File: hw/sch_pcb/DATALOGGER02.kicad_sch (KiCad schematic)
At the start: 0 parts

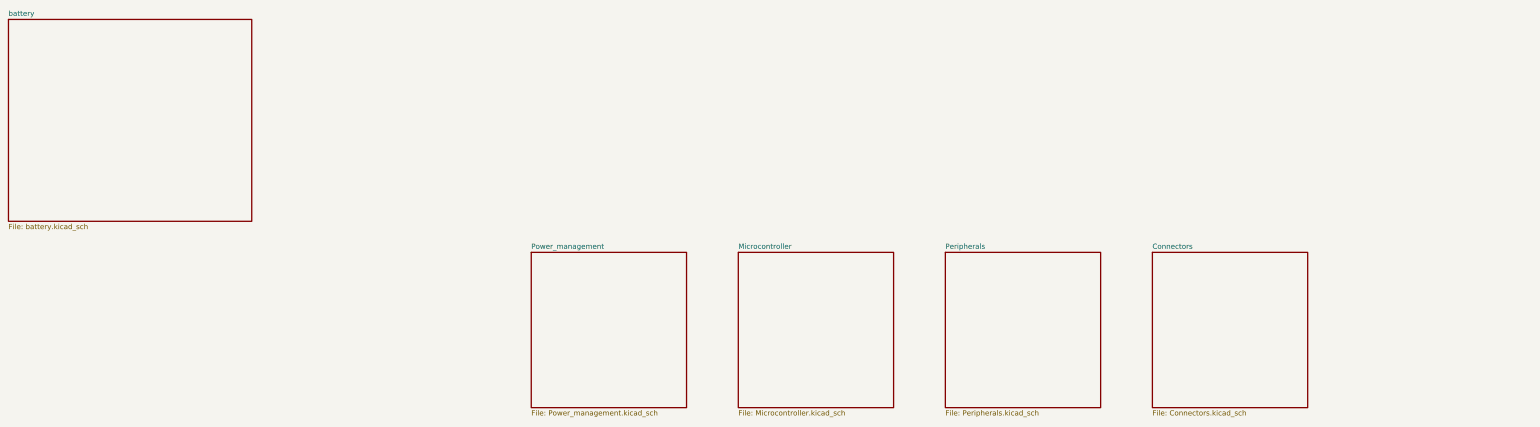
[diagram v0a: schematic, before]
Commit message: Removing Li-ion accumulator BMS Adding ISM02B LoRa telemetry block.
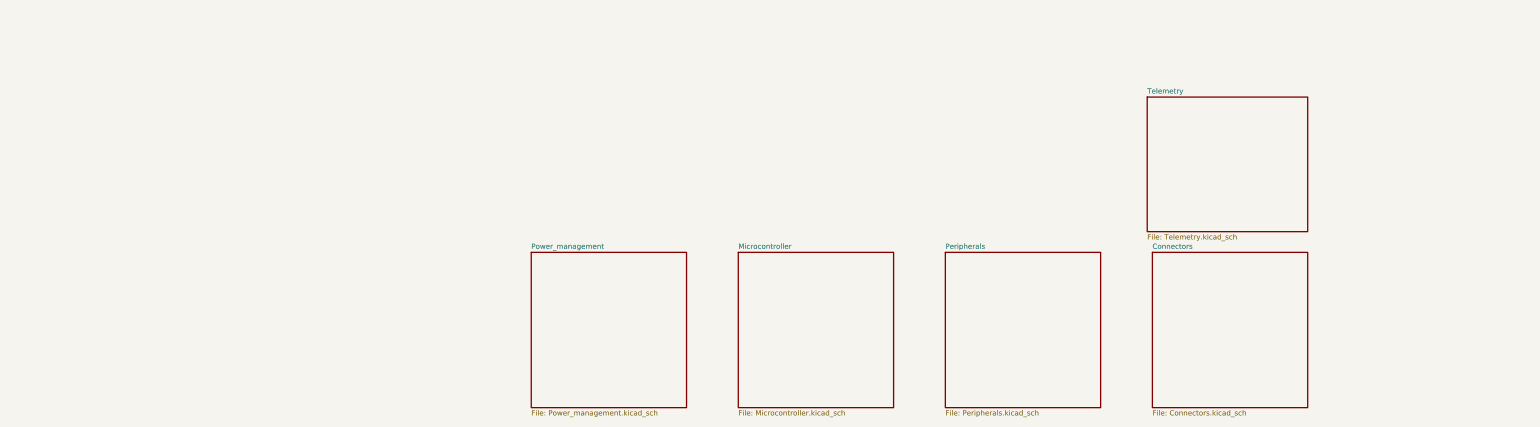
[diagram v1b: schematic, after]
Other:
- removed sheet battery
- added sheet Telemetry (Telemetry.kicad_sch)

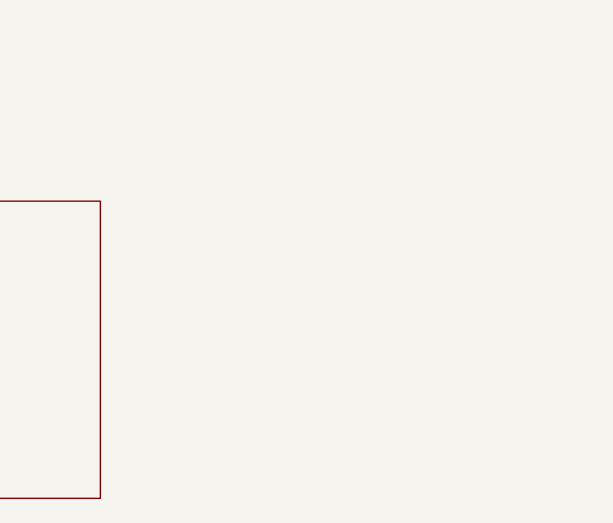
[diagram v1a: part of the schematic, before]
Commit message: schematics update
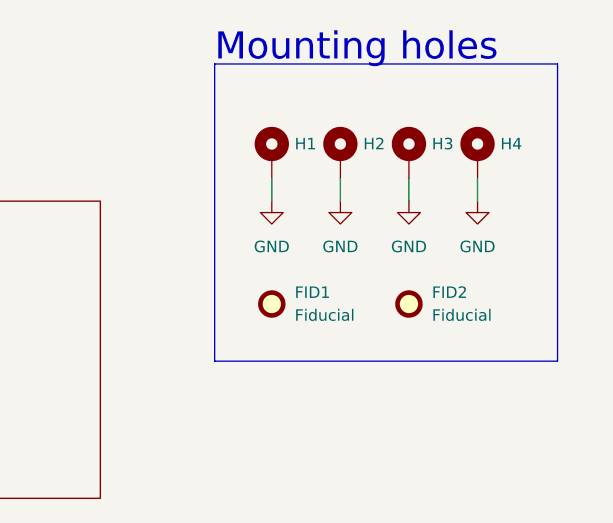
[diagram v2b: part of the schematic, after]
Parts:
- added FID1, FID2: Fiducial, Fiducial:Fiducial_1mm_Mask2mm, symbol Mechanical:Fiducial
- added H1, H2, H3, H4: MountingHole_Pad, Mlab_Mechanical:MountingHole_3mm, symbol Mechanical:MountingHole_Pad
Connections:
- new net GND: H1.1, H2.1, H3.1, H4.1
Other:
- note added: "Mounting holes"
